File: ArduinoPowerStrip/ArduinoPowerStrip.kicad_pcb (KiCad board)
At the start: 2 copper layers, 53.3 x 68.5 mm, 17 parts, among them P101 Con1, P102 Con2, Q101 BC847-SOT23, Q102 BC847-SOT23, U101 MOC3041M, U102 BTA06-600BW, U103 MOC3041M, U104 BTA06-600BW

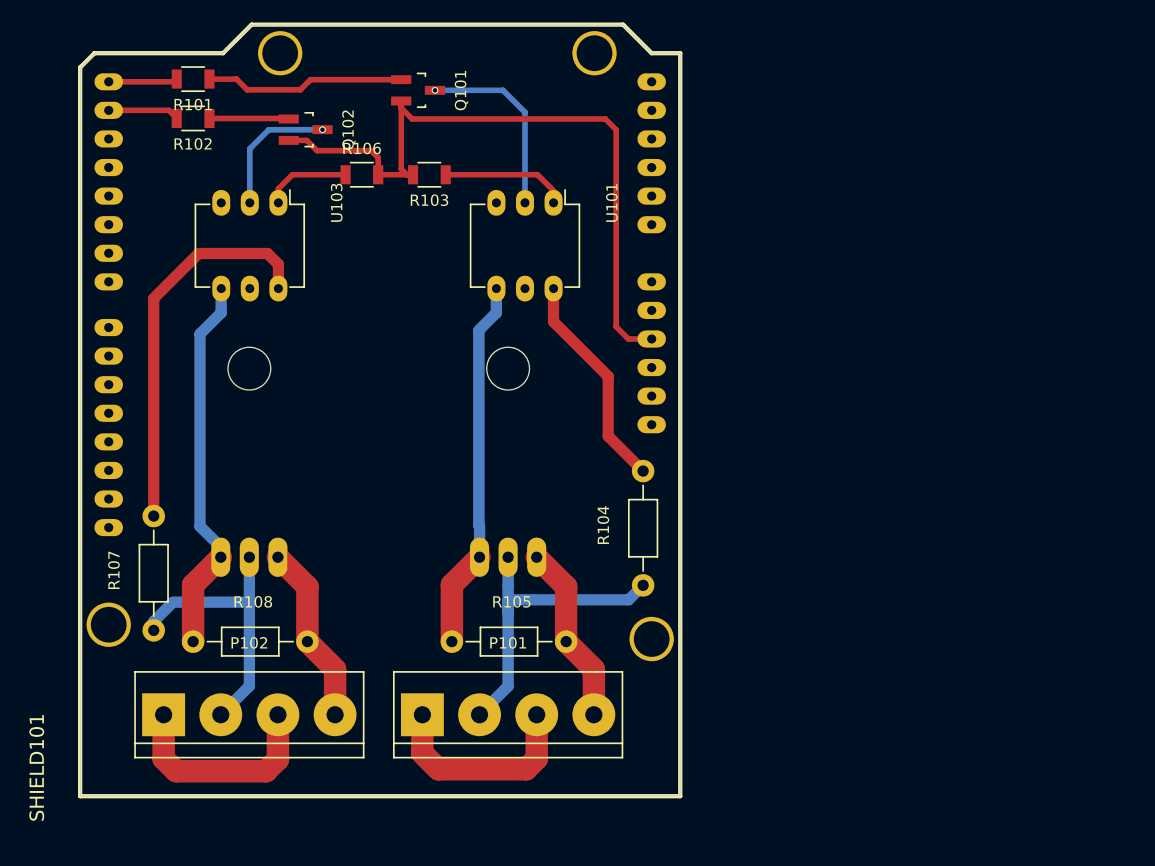
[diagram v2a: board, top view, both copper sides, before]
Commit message: Added LED Indicators
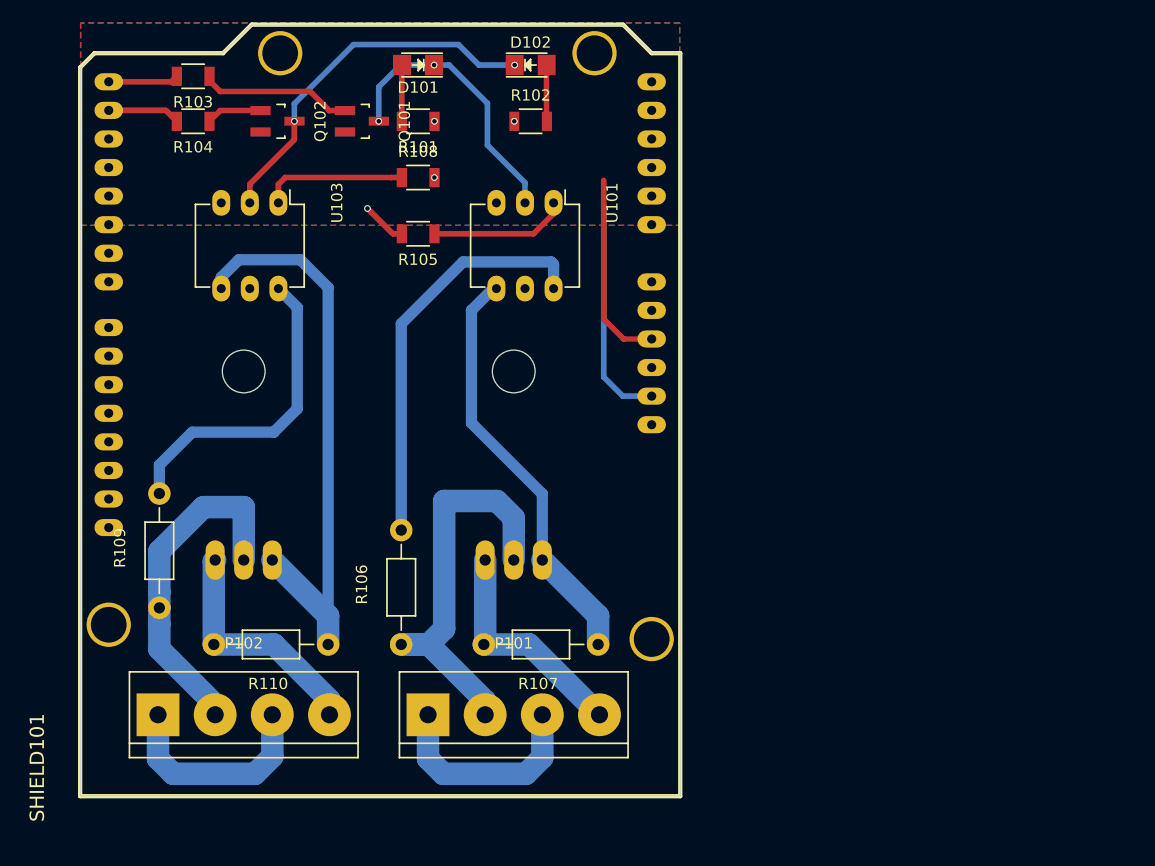
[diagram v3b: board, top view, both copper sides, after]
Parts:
- added D101: LED, LEDs:LED_1206, F.Cu at (100.0, 51.2)
- added D102: LED, LEDs:LED_1206, F.Cu at (110.0, 51.2)
- added R109: 361, Resistors_ThroughHole:Resistor_Horizontal_RM10mm, F.Cu at (77.0, 99.5)
- added R110: 331, Resistors_ThroughHole:Resistor_Horizontal_RM10mm, F.Cu at (92.0, 102.8)
- R103: value 131 -> 331
- R104: value 361 -> 331; footprint Resistors_ThroughHole:Resistor_Horizontal_RM10mm -> Resistors_SMD:R_1206
- R105, R108: value 331 -> 131; footprint Resistors_ThroughHole:Resistor_Horizontal_RM10mm -> Resistors_SMD:R_1206
- R106: value 131 -> 361; footprint Resistors_SMD:R_1206 -> Resistors_ThroughHole:Resistor_Horizontal_RM10mm
- R107: value 361 -> 331
- U102, U104: footprint TO_SOT_Packages_THT:TO-220_Neutral123_Horizontal_LargePads -> TO_SOT_Packages_THT:TO-220_Neutral123_Horizontal_Reverse_LargePads
- moved R104 57.5 mm to (80.0, 56.2), turned to 180 degrees
- moved R108 45.8 mm to (100.0, 61.2)
- moved R106 41.9 mm to (98.5, 102.8), turned to 90 degrees
- moved R107 39.5 mm to (116.0, 102.8), turned to 180 degrees
- moved R105 36.4 mm to (100.0, 66.2), turned to 180 degrees
- moved R102 30.0 mm to (110.0, 56.2), turned to 0 degrees
- moved R103 22.8 mm to (80.0, 52.2)
- moved R101 20.3 mm to (100.0, 56.2)
- moved Q101 5.71 mm to (95.0, 56.2)
- moved Q102 2.61 mm to (87.5, 56.2)
- moved U102 0.56 mm to (108.5, 95.2)
- moved U104 0.56 mm to (84.5, 95.2)
- moved P101 0.50 mm to (108.5, 109.0)
- moved P102 0.50 mm to (84.5, 109.0)
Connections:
- R101 pad 1: Net-(Q101-Pad1) -> /Vcc
- R101 pad 2: /Q1In -> Net-(D101-Pad2)
- R102 pad 1: Net-(Q102-Pad1) -> /Vcc
- R102 pad 2: /Q2In -> Net-(D102-Pad2)
- R103 pad 1: Net-(R103-Pad1) -> Net-(Q101-Pad1)
- R103 pad 2: /Gnd -> /Q1In
- R104 pad 1: /Triac1L -> Net-(Q102-Pad1)
- R104 pad 2: Net-(R104-Pad2) -> /Q2In
- R105 pad 2: /Triac1O -> /Vcc
- R106 pad 1: Net-(R106-Pad1) -> /Triac1L
- R106 pad 2: /Gnd -> Net-(R106-Pad2)
- R107 pad 1: /Triac2L -> Net-(R107-Pad1)
- R107 pad 2: Net-(R107-Pad2) -> /Triac1O
- R108 pad 2: /Triac2O -> /Vcc
- U101 pad 1: Net-(R103-Pad1) -> Net-(R105-Pad1)
- U101 pad 4: Net-(R105-Pad1) -> Net-(R107-Pad1)
- U101 pad 6: Net-(R104-Pad2) -> Net-(R106-Pad2)
- U102 pad 3: Net-(R105-Pad1) -> Net-(R107-Pad1)
- U103 pad 1: Net-(R106-Pad1) -> Net-(R108-Pad1)
- U103 pad 4: Net-(R108-Pad1) -> Net-(R110-Pad1)
- U103 pad 6: Net-(R107-Pad2) -> Net-(R109-Pad2)
- U104 pad 3: Net-(R108-Pad1) -> Net-(R110-Pad1)
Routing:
- net Net-(R110-Pad1): track 0.00 -> 53.4 mm
- net /Gnd: track 61.6 -> 17.3 mm
- net Net-(R107-Pad1): track 0.00 -> 37.4 mm
- net Net-(R106-Pad2): track 0.00 -> 36.4 mm
- net Net-(R107-Pad2): track 34.6 -> 0.00 mm
- net Net-(R109-Pad2): track 0.00 -> 28.2 mm
- net /Vcc: track 0.00 -> 24.7 mm, vias 0 -> 4
- net Net-(R105-Pad1): track 34.0 -> 12.3 mm
- net Net-(R108-Pad1): track 33.9 -> 12.9 mm
- net /Q2Out: track 12.0 -> 33.0 mm, vias 1 -> 2
- net Net-(R104-Pad2): track 19.5 -> 0.00 mm
- net Net-(R103-Pad1): track 11.3 -> 0.00 mm
- net /Triac1L: track 28.8 -> 37.1 mm
- net /Q1Out: track 17.2 -> 25.2 mm, vias 1 -> 2
- net Net-(R106-Pad1): track 7.74 -> 0.00 mm
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- added copper zone on F.Cu, net /Gnd
- added copper zone on B.Cu, net /Vcc
